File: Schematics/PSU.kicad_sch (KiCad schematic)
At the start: 59 parts, among them J2 Upper Cannon, J3 Lower Cannon, J4 7 Volts 2 Amps, J5 7v Return Gnd, J6 +15 Volts 3Amps, J7 ±15 Return Gnd, J8 -15 Volts 3 Amps, J9 Earth Ground, P1 Input Power 120vac, SW1 SW_SPST_Lamp, U1 LM1085-ADJ, U10 Screw_Terminal, U11 Screw_Terminal, U12 Screw_Terminal, U13 Screw_Terminal, U14 Screw_Terminal, U2 LM1085-ADJ, U3 LM1085-ADJ, U4 Screw_Terminal, U5 Screw_Terminal, U6 Screw_Terminal, U7 Screw_Terminal, U8 Screw_Terminal, U9 Screw_Terminal

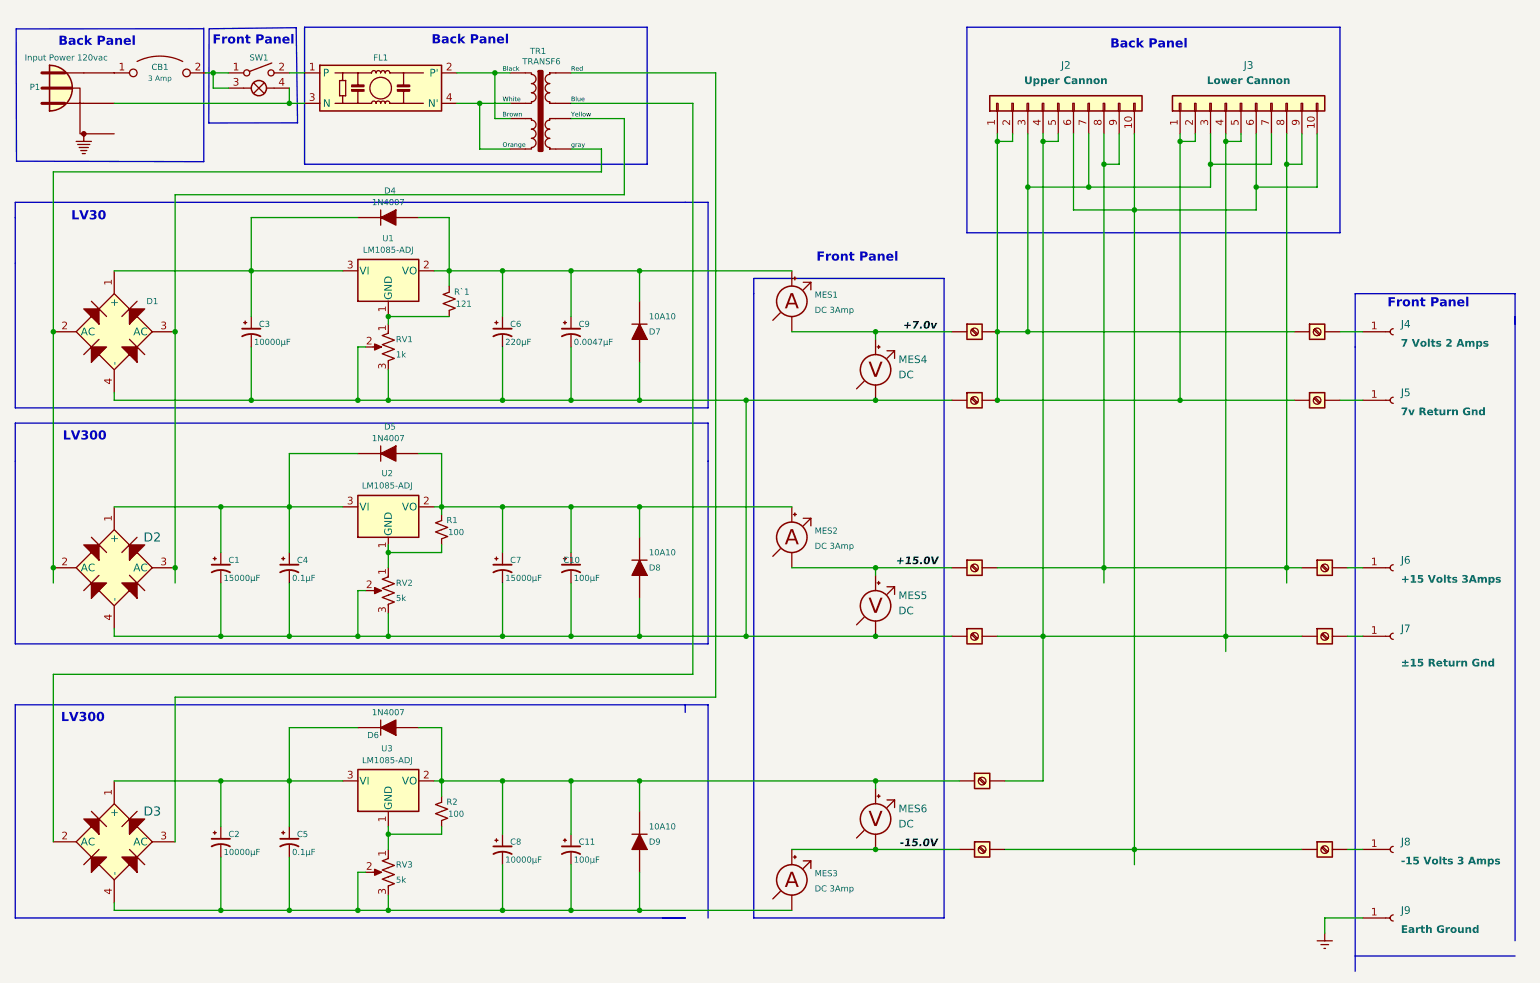
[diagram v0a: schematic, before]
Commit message: Now with dual ESP32 with Midi32 and Disp32.
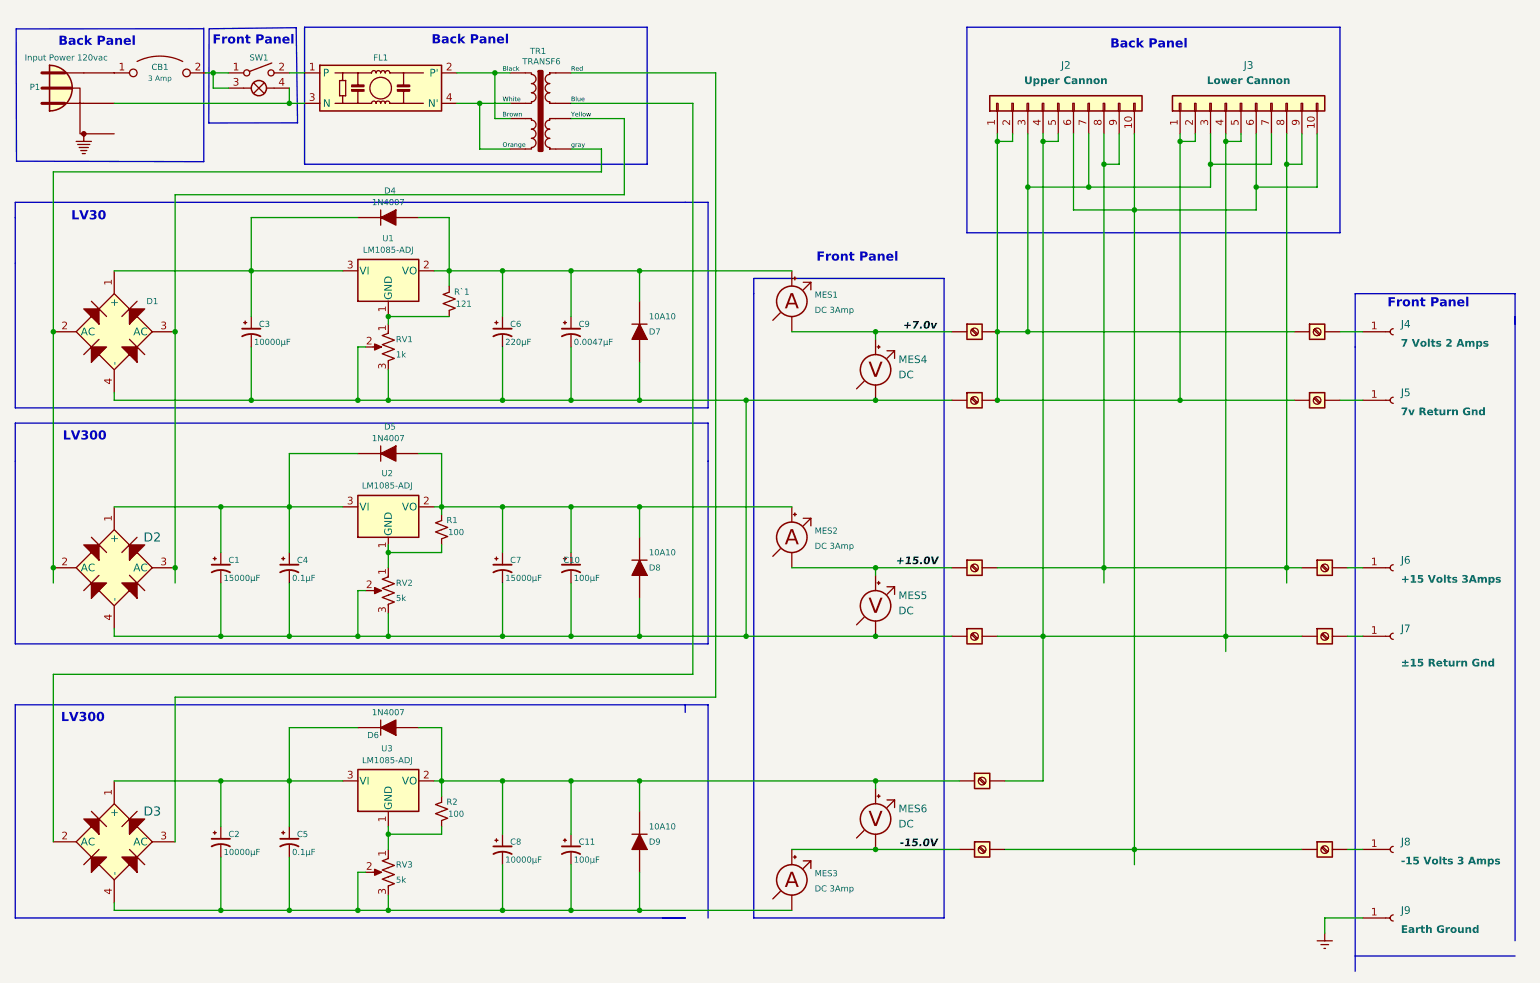
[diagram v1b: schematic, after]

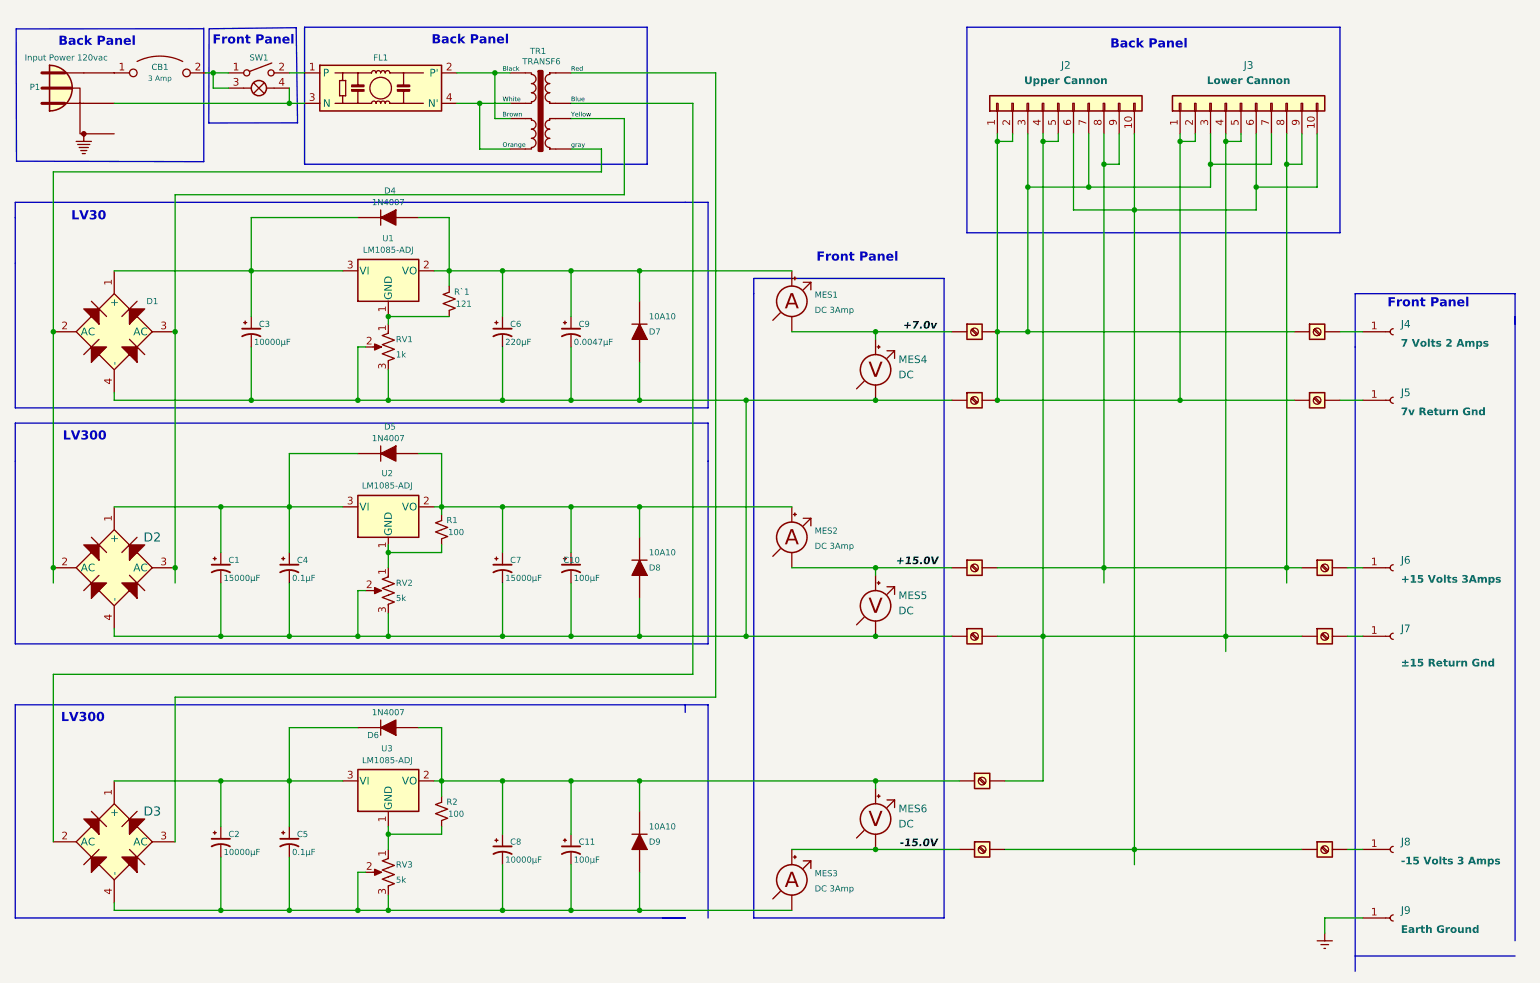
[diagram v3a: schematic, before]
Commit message: adding noise source and variable state filter.
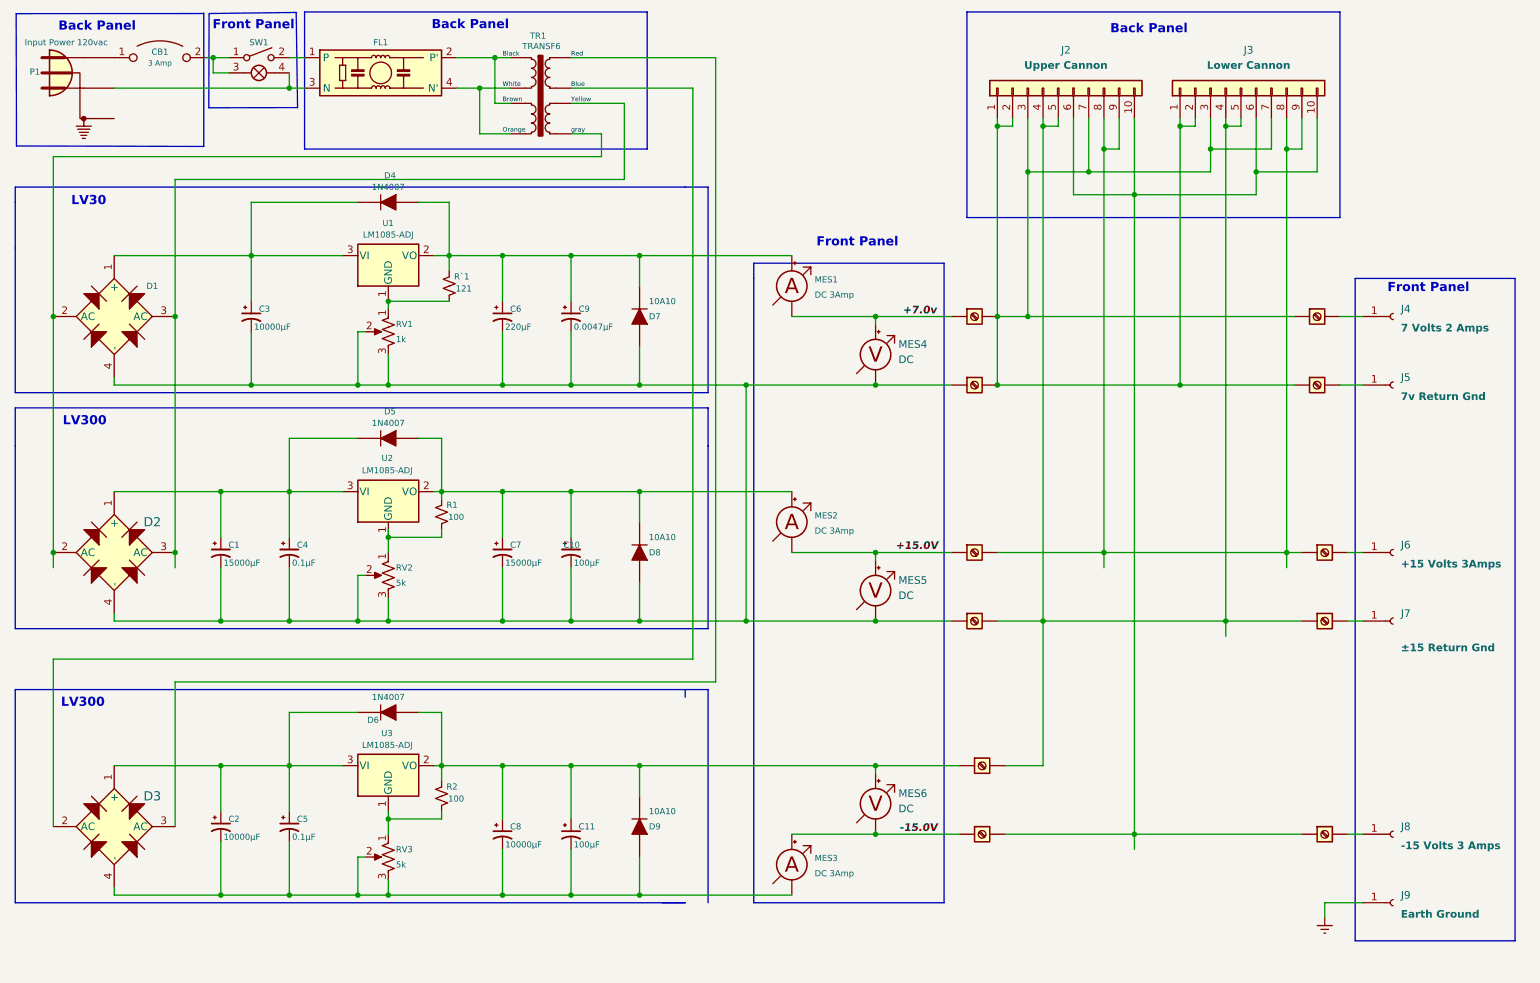
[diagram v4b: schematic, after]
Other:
- moved on the sheet: C1, C10, C11, C2, C3, C4, C5, C6, C7, C8, C9, CB1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

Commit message: Partial software with complete hardware on best 3 state filter with 4 outputs.
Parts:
- renumbered C7 to C?, C9 to C?, C10 to C?, C2 to C?, C11 to C?, C8 to C?, C5 to C?, C1 to C?, C3 to C?, C4 to C?, C6 to C?, CB1 to CB?, D1 to D?, D6 to D?, D5 to D?, D4 to D?, D3 to D?, D7 to D?, D2 to D?, D8 to D?, D9 to D?, FL1 to FL?, J8 to J?, J3 to J?, J6 to J?, J2 to J?, J5 to J?, J9 to J?, J7 to J?, J4 to J?, MES4 to MES?, MES1 to MES?, MES2 to MES?, MES5 to MES?, MES3 to MES?, MES6 to MES?, P1 to P?, R2 to R?, R1 to R?, RV1 to RV?, RV3 to RV?, RV2 to RV?, R`1 to R`?, SW1 to SW?, TR1 to TR?, U14 to U?, U8 to U?, U11 to U?, U6 to U?, U10 to U?, U3 to U?, U12 to U?, U13 to U?, U9 to U?, U4 to U?, U2 to U?, U1 to U?, U5 to U?, U7 to U?
